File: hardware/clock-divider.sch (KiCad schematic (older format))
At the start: 83 parts, among them J1 PWR, J10 PJ-302M, J11 PJ-302M, J12 Conn_01x01, J13 Conn_01x01, J2 Serial debug / programming he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, J3 SPI / ICSP header, J4 PJ-302M, J5 PJ-302M, J6 PJ-302M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

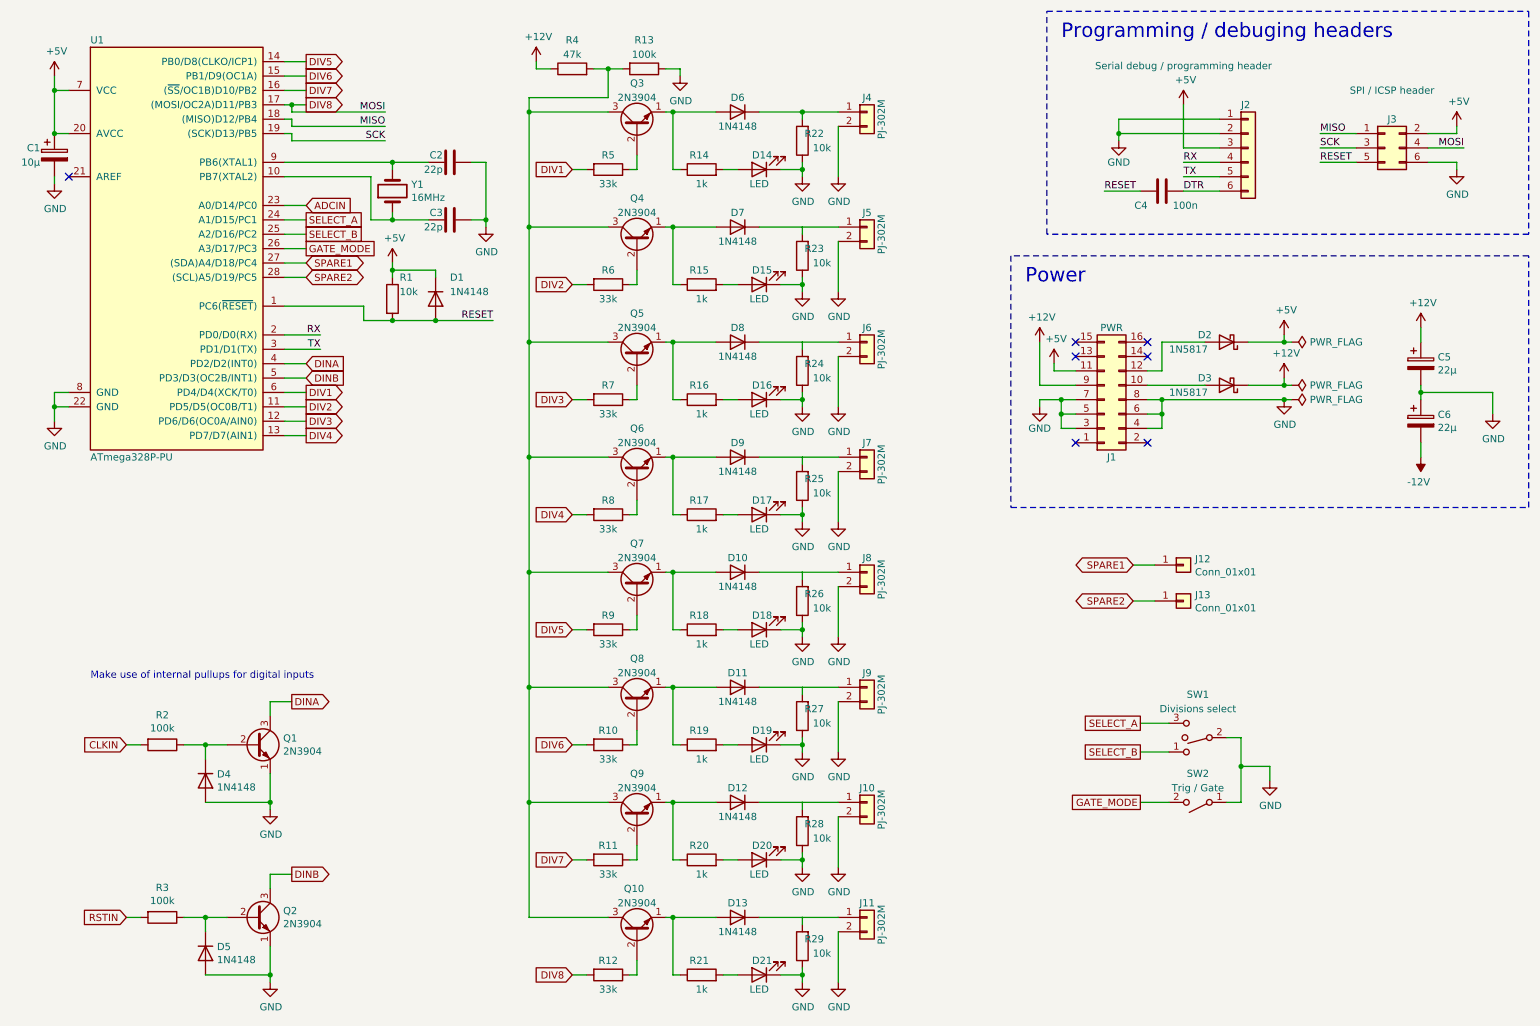
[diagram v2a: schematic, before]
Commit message: Use PJ-302M jack sockets
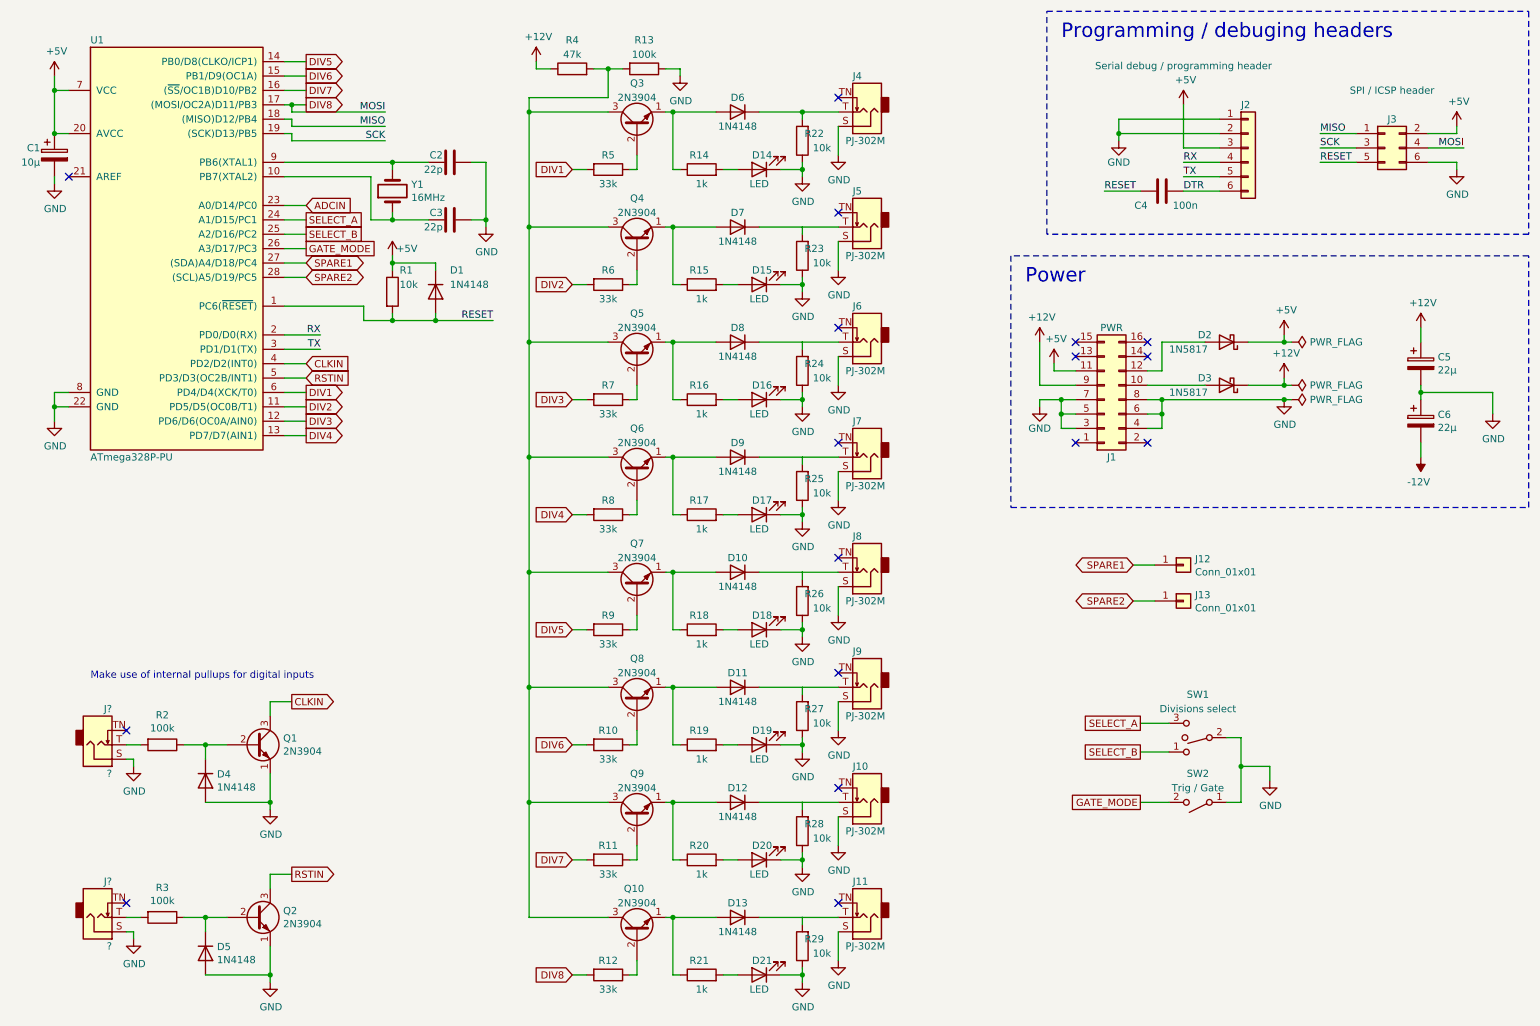
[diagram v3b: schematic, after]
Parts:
- removed J10, J11, J4, J5, J6, J7, J8, J9: PJ-302M, symbol Connector_Generic:Conn_01x02
- added J10, J11, J4, J5, J6, J7, J8, J9: PJ-302M, Custom:PJ-302M_CH, symbol Connector:AudioJack2_SwitchT
- added J? (x2): ?, symbol Connector:AudioJack2_SwitchT
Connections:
- net DINA is gone; now on net CLKIN: Q1.3 (C), U1.4 (PD2/D2(INT0))
- net DINB is gone; now on net RSTIN: Q2.3 (C), U1.5 (PD3/D3(OC2B/INT1))
- net CLKIN: no longer R2.2
- net GND: now also J10.S, J11.S, J4.S, J5.S, J6.S, J7.S, J8.S, J9.S, J?.S, J?.S
- net RSTIN: no longer R3.2
- net at D6.1 (K), R22.2: now also J4.T
- net at D7.1 (K), R23.2: now also J5.T
- net at D8.1 (K), R24.2: now also J6.T
- net at D9.1 (K), R25.2: now also J7.T
- net at D10.1 (K), R26.2: now also J8.T
- net at D11.1 (K), R27.2: now also J9.T
- net at D12.1 (K), R28.2: now also J10.T
- net at D13.1 (K), R29.2: now also J11.T
- new net: J?.T, R2.2
- new net: J?.T, R3.2
- no-connect marks 7 -> 17
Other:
- moved on the sheet: D1, R1

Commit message: Re-allocated µc pins
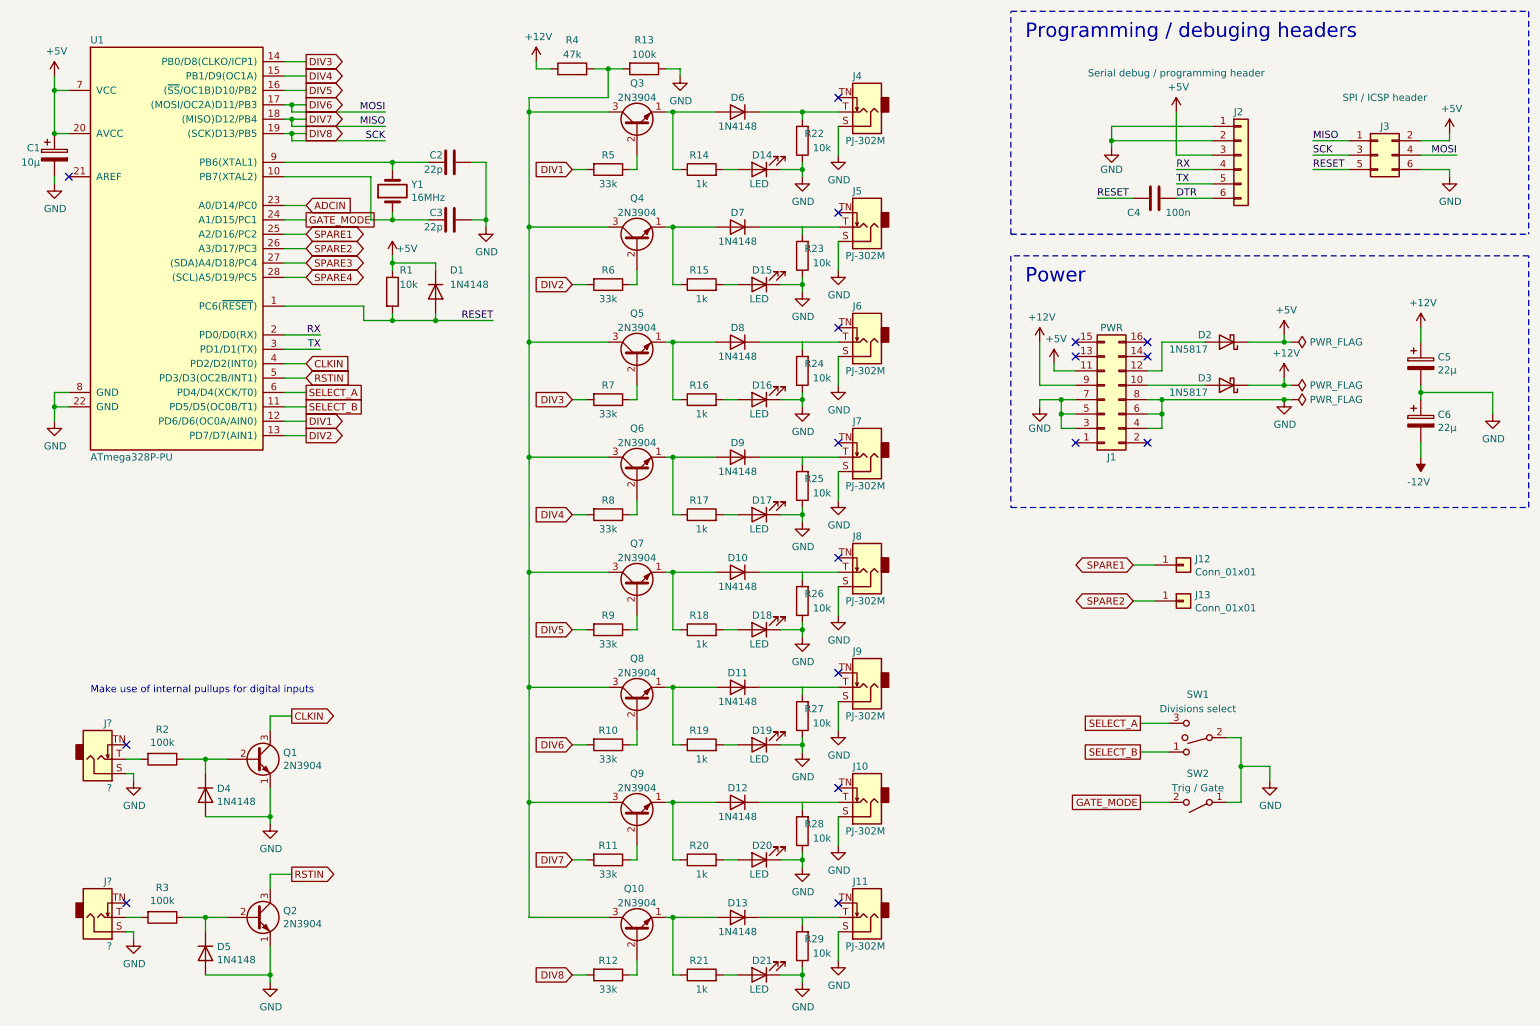
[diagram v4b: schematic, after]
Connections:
- net MISO is gone; now on net DIV7: J3.1 (Pin_1), U1.18 ((MISO)D12/PB4)
- net SCK is gone; now on net DIV8: J3.3 (Pin_3), U1.19 ((SCK)D13/PB5)
- net DIV1: now also U1.12 (PD6/D6(OC0A/AIN0)); no longer U1.6 (PD4/D4(XCK/T0))
- net DIV2: now also U1.13 (PD7/D7(AIN1)); no longer U1.11 (PD5/D5(OC0B/T1))
- net DIV3: now also U1.14 (PB0/D8(CLKO/ICP1)); no longer U1.12 (PD6/D6(OC0A/AIN0))
- net DIV4: now also U1.15 (PB1/D9(OC1A)); no longer U1.13 (PD7/D7(AIN1))
- net DIV5: now also U1.16 ((~SS~/OC1B)D10/PB2); no longer U1.14 (PB0/D8(CLKO/ICP1))
- net DIV6: now also J3.4 (Pin_4), U1.17 ((MOSI/OC2A)D11/PB3); no longer U1.15 (PB1/D9(OC1A))
- net DIV7: no longer U1.16 ((~SS~/OC1B)D10/PB2)
- net DIV8: no longer J3.4 (Pin_4), U1.17 ((MOSI/OC2A)D11/PB3)
- net GATE_MODE: now also U1.24 (A1/D15/PC1); no longer U1.26 (A3/D17/PC3)
- net SELECT_A: now also U1.6 (PD4/D4(XCK/T0)); no longer U1.24 (A1/D15/PC1)
- net SELECT_B: now also U1.11 (PD5/D5(OC0B/T1)); no longer U1.25 (A2/D16/PC2)
- net SPARE1: now also U1.25 (A2/D16/PC2); no longer U1.27 ((SDA)A4/D18/PC4)
- net SPARE2: now also U1.26 (A3/D17/PC3); no longer U1.28 ((SCL)A5/D19/PC5)
- new net SPARE3: U1.27 ((SDA)A4/D18/PC4)
- new net SPARE4: U1.28 ((SCL)A5/D19/PC5)
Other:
- moved on the sheet: C4, D4, J2, J3, J?, Q1, R2

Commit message: outputs are now 0-5V
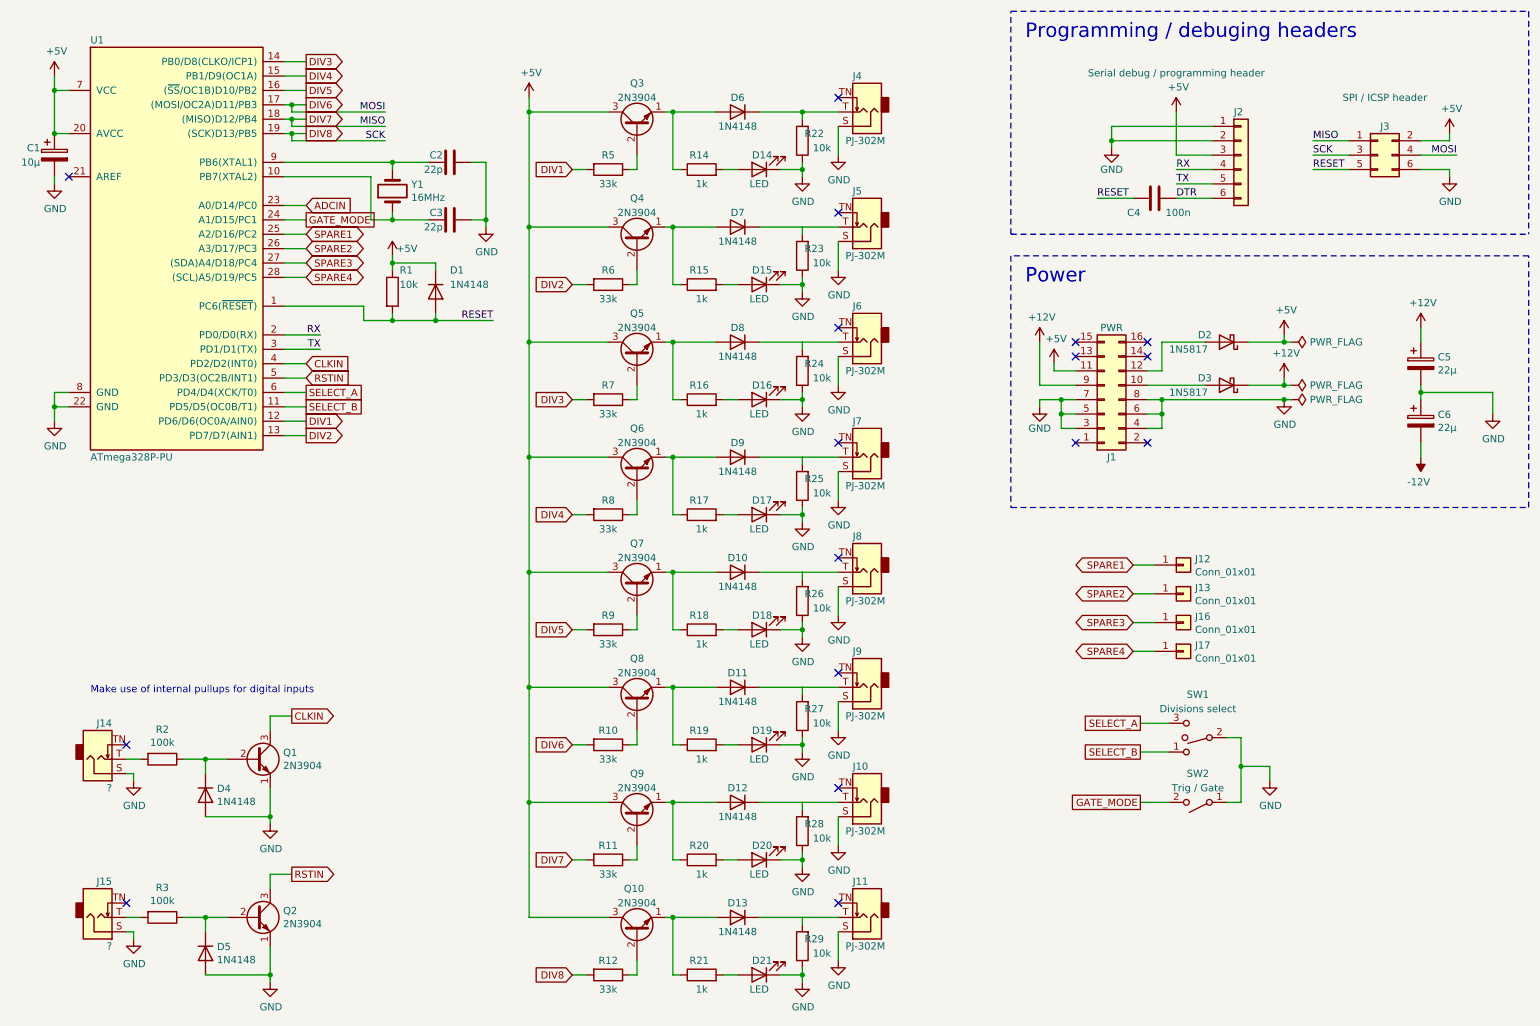
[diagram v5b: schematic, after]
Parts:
- removed R13: 100k, symbol Device:R
- removed R4: 47k, symbol Device:R
- added J16, J17: Conn_01x01, symbol Connector_Generic:Conn_01x01
- gave numbers to parts that had none: 2
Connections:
- net +5V: now also Q10.3 (C), Q3.3 (C), Q4.3 (C), Q5.3 (C), Q6.3 (C), Q7.3 (C), Q8.3 (C), Q9.3 (C)
- net SPARE3: now also J16.1 (Pin_1)
- net SPARE4: now also J17.1 (Pin_1)
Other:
- moved on the sheet: J13
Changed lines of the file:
@@
 Wire Wire Line
 	4650 2100 4100 2100
-$Comp
-L Device:R R4
-U 1 1 6095822A
-P 4400 1000
-F 0 "R4" V 4600 1000 50  0000 C CNN
-F 1 "47k" V 4500 1000 50  0000 C CNN
-F 2 "" V 4330 1000 50  0001 C CNN
-F 3 "~" H 4400 1000 50  0001 C CNN
-	1    4400 1000
-	0    -1   -1   0
-$EndComp
-$Comp
-L Device:R R13
-U 1 1 6095CAC7
-P 4900 1000
-F 0 "R13" V 4700 1000 50  0000 C CNN
-F 1 "100k" V 4800 1000 50  0000 C CNN
-F 2 "" V 4830 1000 50  0001 C CNN
-F 3 "~" H 4900 1000 50  0001 C CNN
-	1    4900 1000
-	0    1    1    0
-$EndComp
-$Comp
-L power:GND #PWR08
-U 1 1 609AAE8E
-P 5150 1050
-F 0 "#PWR08" H 5150 800 50  0001 C CNN
-F 1 "GND" H 5155 877 50  0000 C CNN
-F 2 "" H 5150 1050 50  0001 C CNN
-F 3 "" H 5150 1050 50  0001 C CNN
-	1    5150 1050
-	1    0    0    -1
-$EndComp
-$Comp
-L power:+12V #PWR07
-U 1 1 609BDAC9
-P 4150 950
-F 0 "#PWR07" H 4150 800 50  0001 C CNN
-F 1 "+12V" H 4165 1123 50  0000 C CNN
-F 2 "" H 4150 950 50  0001 C CNN
-F 3 "" H 4150 950 50  0001 C CNN
-	1    4150 950
-	1    0    0    -1
-$EndComp
-Wire Wire Line
-	4150 950  4150 1000
-Wire Wire Line
-	4150 1000 4250 1000
-Wire Wire Line
-	5050 1000 5150 1000
-Wire Wire Line
-	5150 1000 5150 1050
-Wire Wire Line
-	4750 1000 4650 1000
-Wire Wire Line
-	4650 1000 4650 1200
-Wire Wire Line
-	4650 1200 4100 1200
 Wire Wire Line
 	4100 1200 4100 1300
-Connection ~ 4650 1000
-Wire Wire Line
-	4650 1000 4550 1000
 $Comp
 L Connector_Generic:Conn_01x01 J12
@@
 L Connector_Generic:Conn_01x01 J13
 U 1 1 6125E0F2
-P 8650 4700
-F 0 "J13" H 8730 4742 50  0000 L CNN
-F 1 "Conn_01x01" H 8730 4651 50  0000 L CNN
-F 2 "" H 8650 4700 50  0001 C CNN
-F 3 "~" H 8650 4700 50  0001 C CNN
-	1    8650 4700
-	1    0    0    -1
-$EndComp
-Text GLabel 8300 4700 0    50   BiDi ~ 0
+P 8650 4650
+F 0 "J13" H 8730 4692 50  0000 L CNN
+F 1 "Conn_01x01" H 8730 4601 50  0000 L CNN
+F 2 "" H 8650 4650 50  0001 C CNN
+F 3 "~" H 8650 4650 50  0001 C CNN
+	1    8650 4650
+	1    0    0    -1
+$EndComp
+Text GLabel 8300 4650 0    50   BiDi ~ 0
 SPARE2
 Wire Wire Line
-	8300 4700 8450 4700
+	8300 4650 8450 4650
 $Comp
 L Connector:AudioJack2_SwitchT J4
@@
 NoConn ~ 6250 6800
 $Comp
-L Connector:AudioJack2_SwitchT J?
+L Connector:AudioJack2_SwitchT J14
 U 1 1 608CB4E9
 P 1100 5800
-F 0 "J?" H 1200 5550 50  0000 R CNN
+F 0 "J14" H 1200 5550 50  0000 R CNN
 F 1 "?" H 1200 6000 50  0000 R CNN
 F 2 "" H 1100 5800 50  0001 C CNN
@@
 NoConn ~ 1300 5700
 $Comp
-L Connector:AudioJack2_SwitchT J?
+L Connector:AudioJack2_SwitchT J15
 U 1 1 609BEA9C
 P 1100 6900
-F 0 "J?" H 1200 6650 50  0000 R CNN
+F 0 "J15" H 1200 6650 50  0000 R CNN
 F 1 "?" H 1200 7100 50  0000 R CNN
 F 2 "" H 1100 6900 50  0001 C CNN
@@
 Text GLabel 2550 2450 2    50   BiDi ~ 0
 SPARE4
+$Comp
+L Connector_Generic:Conn_01x01 J16
+U 1 1 60C26DA1
+P 8650 4850
+F 0 "J16" H 8730 4892 50  0000 L CNN
+F 1 "Conn_01x01" H 8730 4801 50  0000 L CNN
+F 2 "" H 8650 4850 50  0001 C CNN
+F 3 "~" H 8650 4850 50  0001 C CNN
+	1    8650 4850
+	1    0    0    -1
+$EndComp
+Text GLabel 8300 4850 0    50   BiDi ~ 0
+SPARE3
+Wire Wire Line
+	8300 4850 8450 4850
+$Comp
+L Connector_Generic:Conn_01x01 J17
+U 1 1 60C42635
+P 8650 5050
+F 0 "J17" H 8730 5092 50  0000 L CNN
+F 1 "Conn_01x01" H 8730 5001 50  0000 L CNN
+F 2 "" H 8650 5050 50  0001 C CNN
+F 3 "~" H 8650 5050 50  0001 C CNN
+	1    8650 5050
+	1    0    0    -1
+$EndComp
+Text GLabel 8300 5050 0    50   BiDi ~ 0
+SPARE4
+Wire Wire Line
+	8300 5050 8450 5050
+$Comp
+L power:+5V #PWR?
+U 1 1 60C7A5C0
+P 4100 1200
+F 0 "#PWR?" H 4100 1050 50  0001 C CNN
+F 1 "+5V" H 4115 1373 50  0000 C CNN
+F 2 "" H 4100 1200 50  0001 C CNN
+F 3 "" H 4100 1200 50  0001 C CNN
+	1    4100 1200
+	1    0    0    -1
+$EndComp
 $EndSCHEMATC
